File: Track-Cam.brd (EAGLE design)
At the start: 65 x 56 mm, 37 parts, among them IC1 STM32F042KT/M, IC2 BD6211F/M, IC3 BD6211F/M, X1 RASPI_BOARD_B+#_HC

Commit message: optimized grand path
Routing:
- net GND: track 196.2 -> 213.5 mm, vias 3 -> 1
- net SWDIO: track 20.4 -> 18.5 mm
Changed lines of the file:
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@@
 <contactref element="IC1" pad="23"/>
 <contactref element="X1" pad="18"/>
-<wire x1="36.195" y1="42.672" x2="42.1386" y2="42.672" width="0.1524" layer="1"/>
-<wire x1="34.671" y1="44.196" x2="36.195" y2="42.672" width="0.1524" layer="1"/>
-<wire x1="34.29" y1="44.196" x2="34.671" y2="44.196" width="0.1524" layer="1"/>
-<wire x1="29.8704" y1="48.6156" x2="34.29" y2="44.196" width="0.1524" layer="1"/>
-<wire x1="29.8704" y1="52.578" x2="29.8704" y2="48.6156" width="0.1524" layer="16"/>
+<wire x1="40.6908" y1="42.672" x2="42.1386" y2="42.672" width="0.1524" layer="1"/>
+<wire x1="32.385" y1="50.9778" x2="40.6908" y2="42.672" width="0.1524" layer="16"/>
+<wire x1="32.385" y1="51.6636" x2="32.385" y2="50.9778" width="0.1524" layer="16"/>
+<wire x1="31.4706" y1="52.578" x2="32.385" y2="51.6636" width="0.1524" layer="16"/>
+<wire x1="29.8704" y1="52.578" x2="31.4706" y2="52.578" width="0.1524" layer="16"/>
 <wire x1="28.7274" y1="53.721" x2="29.8704" y2="52.578" width="0.1524" layer="16"/>
 <wire x1="42.1386" y1="42.672" x2="42.14" y2="42.64" width="0.1524" layer="1"/>
 <wire x1="28.7274" y1="53.721" x2="28.69" y2="53.77" width="0.1524" layer="16"/>
-<via x="29.8704" y="48.6156" extent="1-16" drill="0.3048"/>
+<via x="40.6908" y="42.672" extent="1-16" drill="0.3048"/>
 </signal>
 <signal name="SWCLK">
@@
 <wire x1="53.1876" y1="47.7774" x2="52.945" y2="47.625" width="0.6096" layer="1"/>
 <wire x1="56.6166" y1="51.2064" x2="56.63" y2="51.23" width="0.6096" layer="1"/>
-<wire x1="32.5374" y1="47.3964" x2="32.5374" y2="48.5394" width="0.6096" layer="1"/>
-<wire x1="34.5948" y1="45.339" x2="33.7185" y2="46.2153" width="0.6096" layer="1"/>
-<wire x1="33.7185" y1="46.2153" x2="32.5374" y2="47.3964" width="0.6096" layer="1"/>
-<wire x1="32.5374" y1="48.5394" x2="32.4625" y2="48.5775" width="0.6096" layer="1"/>
-<wire x1="34.5948" y1="45.339" x2="34.665" y2="45.315" width="0.6096" layer="1"/>
-<wire x1="33.9852" y1="46.4058" x2="33.909" y2="46.4058" width="0.6096" layer="1"/>
-<wire x1="38.7858" y1="51.2064" x2="33.9852" y2="46.4058" width="0.6096" layer="16"/>
-<wire x1="33.909" y1="46.4058" x2="33.7185" y2="46.2153" width="0.6096" layer="1"/>
-<wire x1="38.7858" y1="51.2064" x2="38.85" y2="51.23" width="0.6096" layer="16"/>
 <wire x1="50.8254" y1="49.8348" x2="52.8066" y2="47.8536" width="0.6096" layer="1"/>
 <wire x1="40.2336" y1="49.8348" x2="50.8254" y2="49.8348" width="0.6096" layer="1"/>
@@
 <wire x1="13.335" y1="37.465" x2="13.335" y2="37.8714" width="0.6096" layer="16"/>
 <wire x1="18.5166" y1="51.2064" x2="18.53" y2="51.23" width="0.6096" layer="16"/>
-<wire x1="31.3944" y1="46.2534" x2="33.7566" y2="46.2534" width="0.6096" layer="16"/>
-<wire x1="30.099" y1="46.2534" x2="31.3944" y2="46.2534" width="0.6096" layer="1"/>
-<wire x1="33.7566" y1="46.2534" x2="33.9852" y2="46.4058" width="0.6096" layer="16"/>
-<wire x1="30.099" y1="46.2534" x2="29.845" y2="46.085" width="0.6096" layer="1"/>
 <wire x1="56.6166" y1="35.8902" x2="50.1396" y2="29.4132" width="0.6096" layer="16"/>
 <wire x1="56.6166" y1="51.2064" x2="56.6166" y2="35.8902" width="0.6096" layer="16"/>
@@
 <wire x1="56.6166" y1="51.2064" x2="56.63" y2="51.23" width="0.6096" layer="16"/>
 <via x="51.435" y="17.2212" extent="1-16" drill="0.3048"/>
-<via x="33.9852" y="46.4058" extent="1-16" drill="0.3048"/>
-<via x="31.3944" y="46.2534" extent="1-16" drill="0.3048"/>
+<wire x1="40.0812" y1="33.6804" x2="40.0812" y2="34.4424" width="0.6096" layer="1"/>
+<wire x1="44.2722" y1="29.4894" x2="40.0812" y2="33.6804" width="0.6096" layer="1"/>
+<wire x1="44.2722" y1="22.3266" x2="44.2722" y2="29.4894" width="0.6096" layer="1"/>
+<wire x1="48.2346" y1="18.3642" x2="44.2722" y2="22.3266" width="0.6096" layer="1"/>
+<wire x1="48.2346" y1="16.1544" x2="48.2346" y2="18.3642" width="0.6096" layer="1"/>
+<wire x1="48.768" y1="15.621" x2="48.2346" y2="16.1544" width="0.6096" layer="1"/>
+<wire x1="51.2064" y1="15.621" x2="48.768" y2="15.621" width="0.6096" layer="1"/>
+<wire x1="40.0812" y1="34.4424" x2="39.9288" y2="34.671" width="0.6096" layer="1"/>
+<wire x1="51.2064" y1="15.621" x2="51.435" y2="15.7734" width="0.6096" layer="1"/>
+<wire x1="30.099" y1="46.1772" x2="31.9278" y2="48.006" width="0.6096" layer="1"/>
+<wire x1="31.9278" y1="48.006" x2="32.4612" y2="48.5394" width="0.6096" layer="1"/>
+<wire x1="32.4612" y1="48.5394" x2="32.4625" y2="48.5775" width="0.6096" layer="1"/>
+<wire x1="30.099" y1="46.1772" x2="29.845" y2="46.085" width="0.6096" layer="1"/>
+<wire x1="31.9278" y1="48.006" x2="34.5948" y2="45.339" width="0.6096" layer="1"/>
+<wire x1="34.5948" y1="45.339" x2="34.665" y2="45.315" width="0.6096" layer="1"/>
 </signal>
 <signal name="MOTOR2_POS">

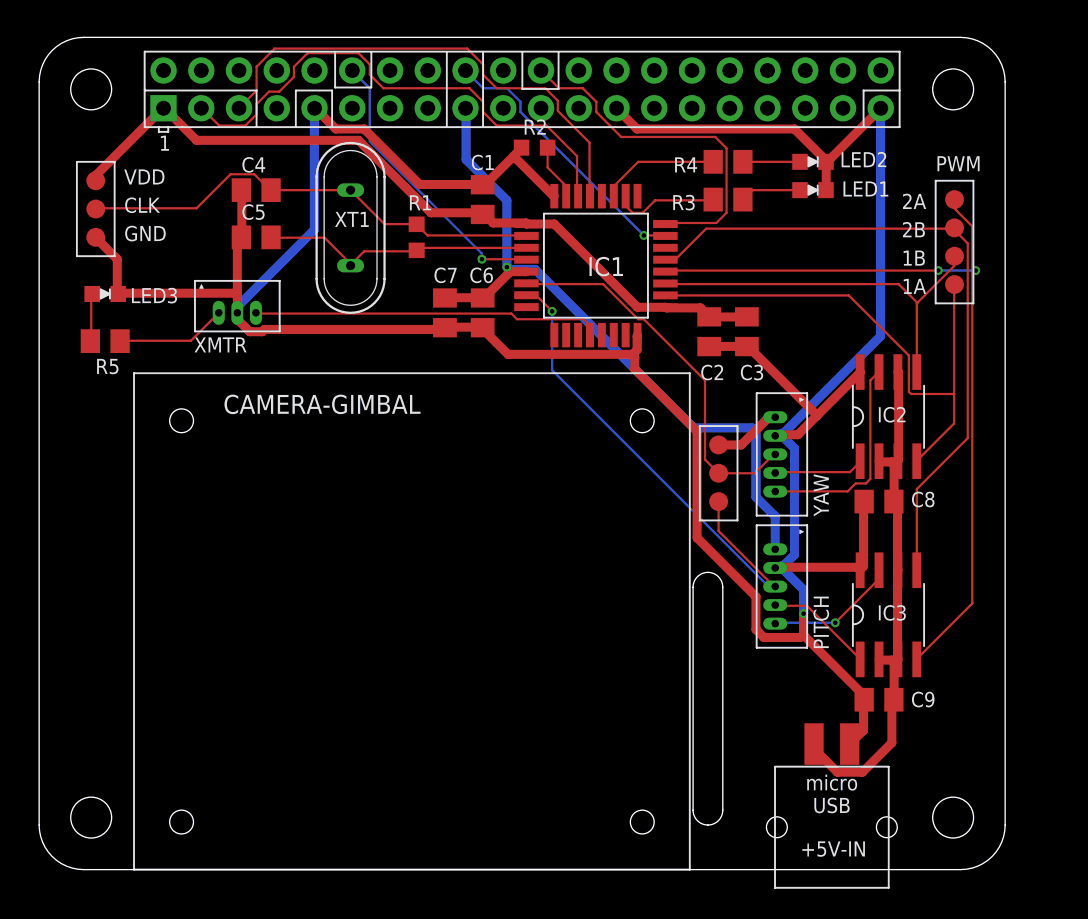
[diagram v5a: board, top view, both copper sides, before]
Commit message: apply solid wiring
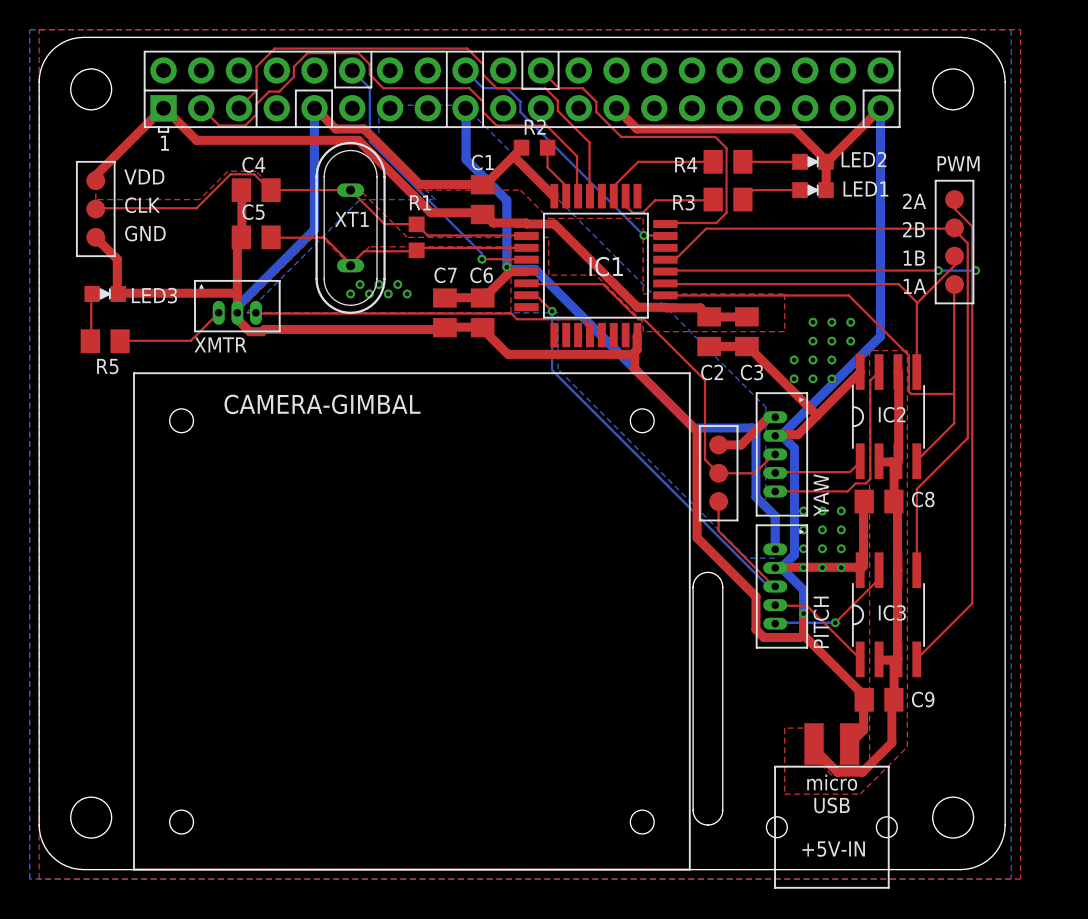
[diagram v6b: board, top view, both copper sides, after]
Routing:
- net GND: vias 1 -> 25
- net +3V3: vias 1 -> 8
- added copper zone on layer 1, net +3V3
- added copper zone on layer 16, net +3V3
- added copper zone on layer 1, net +5V
- added copper zone on layer 1, net GND
- added copper zone on layer 16, net GND
- added copper zone on layer 1, net VDD
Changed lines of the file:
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@@
 <layers>
 <layer number="1" name="Top" color="4" fill="1" visible="yes" active="yes"/>
-<layer number="16" name="Bottom" color="1" fill="1" visible="yes" active="yes"/>
+<layer number="16" name="Bottom" color="1" fill="1" visible="no" active="yes"/>
 <layer number="17" name="Pads" color="2" fill="1" visible="yes" active="yes"/>
 <layer number="18" name="Vias" color="2" fill="1" visible="yes" active="yes"/>
@@
 <wire x1="34.665" y1="43.44" x2="40.265" y2="37.84" width="0.6096" layer="1"/>
 <wire x1="40.265" y1="37.84" x2="42.14" y2="37.84" width="0.6096" layer="1"/>
+<polygon width="0.6096" layer="1" spacing="1.778" isolate="0.2032" thermals="no">
+<vertex x="3.81" y="46.355"/>
+<vertex x="8.255" y="50.8"/>
+<vertex x="8.89" y="50.8"/>
+<vertex x="10.795" y="48.895"/>
+<vertex x="21.59" y="48.895"/>
+<vertex x="23.495" y="46.99"/>
+<vertex x="24.765" y="45.72"/>
+<vertex x="32.385" y="45.72"/>
+<vertex x="34.29" y="43.815"/>
+<vertex x="40.64" y="43.815"/>
+<vertex x="40.64" y="38.735"/>
+<vertex x="50.165" y="38.735"/>
+<vertex x="50.165" y="36.195"/>
+<vertex x="41.275" y="36.195"/>
+<vertex x="40.64" y="36.195"/>
+<vertex x="40.64" y="36.83"/>
+<vertex x="37.465" y="40.005"/>
+<vertex x="34.29" y="40.005"/>
+<vertex x="34.29" y="42.545"/>
+<vertex x="24.765" y="42.545"/>
+<vertex x="21.59" y="45.72"/>
+<vertex x="15.875" y="45.72"/>
+<vertex x="14.605" y="46.99"/>
+<vertex x="12.7" y="46.99"/>
+<vertex x="10.795" y="45.085"/>
+<vertex x="3.81" y="45.085"/>
+</polygon>
 </signal>
 <signal name="OSC_IN">
@@
 <wire x1="31.6992" y1="40.386" x2="31.4706" y2="40.5384" width="0.6096" layer="16"/>
 <via x="31.4706" y="40.5384" extent="1-16" drill="0.3048"/>
+<polygon width="0.6096" layer="1" spacing="1.778" isolate="0.2032" thermals="no" rank="2">
+<vertex x="19.05" y="42.545"/>
+<vertex x="18.415" y="42.545"/>
+<vertex x="13.335" y="37.465"/>
+<vertex x="31.75" y="37.465"/>
+<vertex x="31.75" y="41.91"/>
+<vertex x="22.225" y="41.91"/>
+<vertex x="20.955" y="40.64"/>
+</polygon>
+<polygon width="0.6096" layer="16" spacing="1.778" isolate="0.3048" thermals="no">
+<vertex x="28.575" y="51.435"/>
+<vertex x="48.895" y="31.115"/>
+<vertex x="48.895" y="24.765"/>
+<vertex x="49.53" y="24.13"/>
+<vertex x="49.53" y="20.955"/>
+<vertex x="47.625" y="20.955"/>
+<vertex x="34.925" y="33.655"/>
+<vertex x="34.925" y="37.465"/>
+<vertex x="13.97" y="37.465"/>
+<vertex x="21.59" y="45.085"/>
+<vertex x="26.67" y="45.085"/>
+<vertex x="22.86" y="48.895"/>
+<vertex x="22.86" y="51.435"/>
+</polygon>
+<via x="20.955" y="38.735" extent="1-16" drill="0.3048"/>
+<via x="21.59" y="39.37" extent="1-16" drill="0.3048"/>
+<via x="22.225" y="38.735" extent="1-16" drill="0.3048"/>
+<via x="22.86" y="39.37" extent="1-16" drill="0.3048"/>
+<via x="23.495" y="38.735" extent="1-16" drill="0.3048"/>
+<via x="24.13" y="39.37" extent="1-16" drill="0.3048"/>
+<via x="24.765" y="38.735" extent="1-16" drill="0.3048"/>
 </signal>
 <signal name="BOOT0">
@@
 <wire x1="57.7596" y1="14.4018" x2="57.785" y2="14.145" width="0.6096" layer="1"/>
 <wire x1="57.7596" y1="19.8882" x2="57.785" y2="20.145" width="0.6096" layer="1"/>
+<polygon width="0.6096" layer="1" spacing="1.778" isolate="0.2032" thermals="no" rank="2">
+<vertex x="55.245" y="6.35"/>
+<vertex x="53.34" y="6.35"/>
+<vertex x="52.705" y="6.985"/>
+<vertex x="52.705" y="9.525"/>
+<vertex x="50.165" y="9.525"/>
+<vertex x="50.165" y="5.08"/>
+<vertex x="55.245" y="5.08"/>
+<vertex x="58.42" y="8.255"/>
+<vertex x="58.42" y="34.925"/>
+<vertex x="55.88" y="34.925"/>
+<vertex x="55.88" y="7.62"/>
+<vertex x="55.88" y="6.985"/>
+</polygon>
 </signal>
 <signal name="MOTOR1+">
@@
 <wire x1="31.9278" y1="48.006" x2="34.5948" y2="45.339" width="0.6096" layer="1"/>
 <wire x1="34.5948" y1="45.339" x2="34.665" y2="45.315" width="0.6096" layer="1"/>
+<polygon width="0.6096" layer="1" spacing="1.778" isolate="0.3048" thermals="no" rank="6">
+<vertex x="0" y="56.515"/>
+<vertex x="66.04" y="56.515"/>
+<vertex x="66.04" y="-0.635"/>
+<vertex x="0" y="-0.635"/>
+</polygon>
+<polygon width="0.6096" layer="16" spacing="1.778" isolate="0.3048" thermals="no" rank="6">
+<vertex x="-0.635" y="56.515"/>
+<vertex x="65.405" y="56.515"/>
+<vertex x="65.405" y="-0.635"/>
+<vertex x="-0.635" y="-0.635"/>
+</polygon>
+<via x="52.07" y="36.83" extent="1-16" drill="0.3048"/>
+<via x="53.34" y="36.83" extent="1-16" drill="0.3048"/>
+<via x="54.61" y="36.83" extent="1-16" drill="0.3048"/>
+<via x="54.61" y="35.56" extent="1-16" drill="0.3048"/>
+<via x="53.34" y="35.56" extent="1-16" drill="0.3048"/>
+<via x="52.07" y="35.56" extent="1-16" drill="0.3048"/>
+<via x="50.8" y="34.29" extent="1-16" drill="0.3048"/>
+<via x="52.07" y="34.29" extent="1-16" drill="0.3048"/>
+<via x="53.34" y="34.29" extent="1-16" drill="0.3048"/>
+<via x="53.34" y="33.02" extent="1-16" drill="0.3048"/>
+<via x="52.07" y="33.02" extent="1-16" drill="0.3048"/>
+<via x="50.8" y="33.02" extent="1-16" drill="0.3048"/>
+<via x="51.435" y="24.13" extent="1-16" drill="0.3048"/>
+<via x="52.705" y="24.13" extent="1-16" drill="0.3048"/>
+<via x="53.975" y="24.13" extent="1-16" drill="0.3048"/>
+<via x="53.975" y="22.86" extent="1-16" drill="0.3048"/>
+<via x="52.705" y="22.86" extent="1-16" drill="0.3048"/>
+<via x="51.435" y="22.86" extent="1-16" drill="0.3048"/>
+<via x="51.435" y="21.59" extent="1-16" drill="0.3048"/>
+<via x="52.705" y="21.59" extent="1-16" drill="0.3048"/>
+<via x="53.975" y="21.59" extent="1-16" drill="0.3048"/>
+<via x="53.975" y="20.32" extent="1-16" drill="0.3048"/>
+<via x="52.705" y="20.32" extent="1-16" drill="0.3048"/>
+<via x="51.435" y="20.32" extent="1-16" drill="0.3048"/>
 </signal>
 <signal name="MOTOR2_POS">
